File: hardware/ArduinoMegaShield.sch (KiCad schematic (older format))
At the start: 54 parts, among them P1 CONN_01X02, P10 CONN_01X02, P11 CONN_01X02, P12 CONN_01X02, P13 CONN_01X02, P14 CONN_01X02, P15 CONN_01X02, P16 CONN_01X02, P18 CONN_01X02, P2 CONN_01X02, P3 CONN_01X02, P4 CONN_01X02, P5 CONN_01X02, P6 CONN_01X02, P7 CONN_01X02, P8 CONN_01X02, P9 CONN_01X02, U1 A4988, U2 A4988, U3 A4988

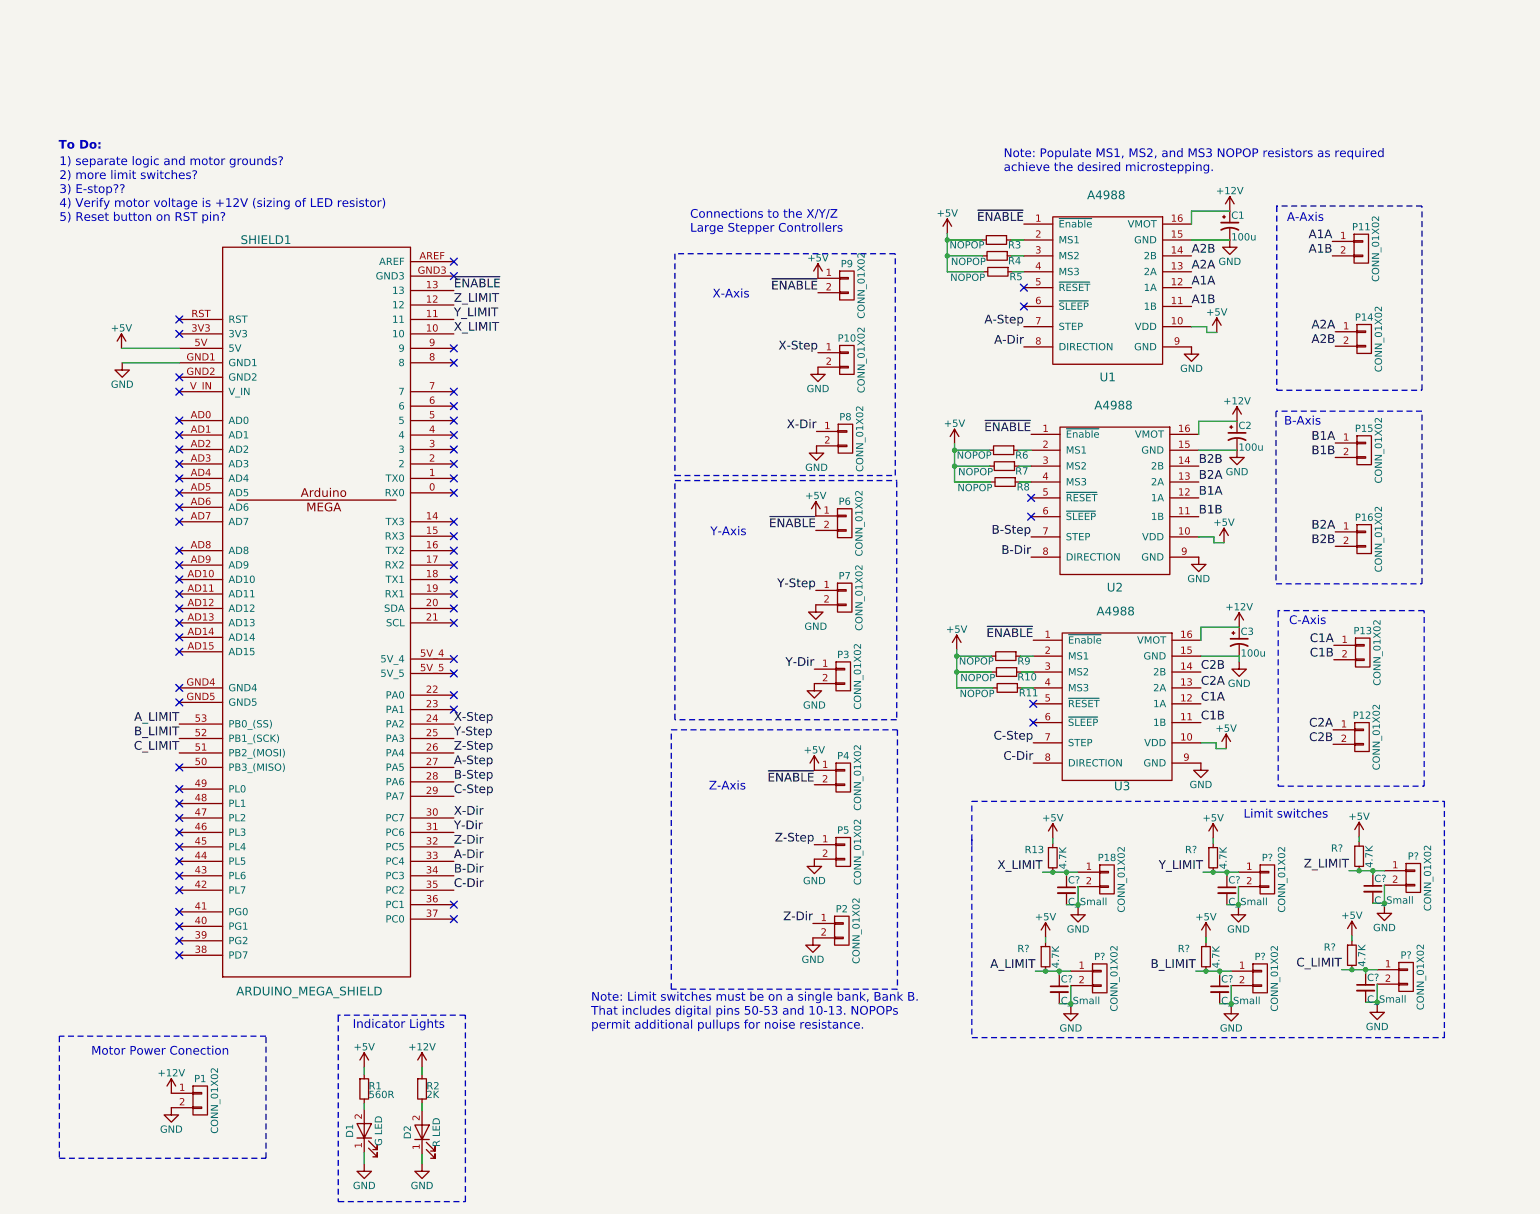
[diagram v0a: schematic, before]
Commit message: added estop on the avr reset pin
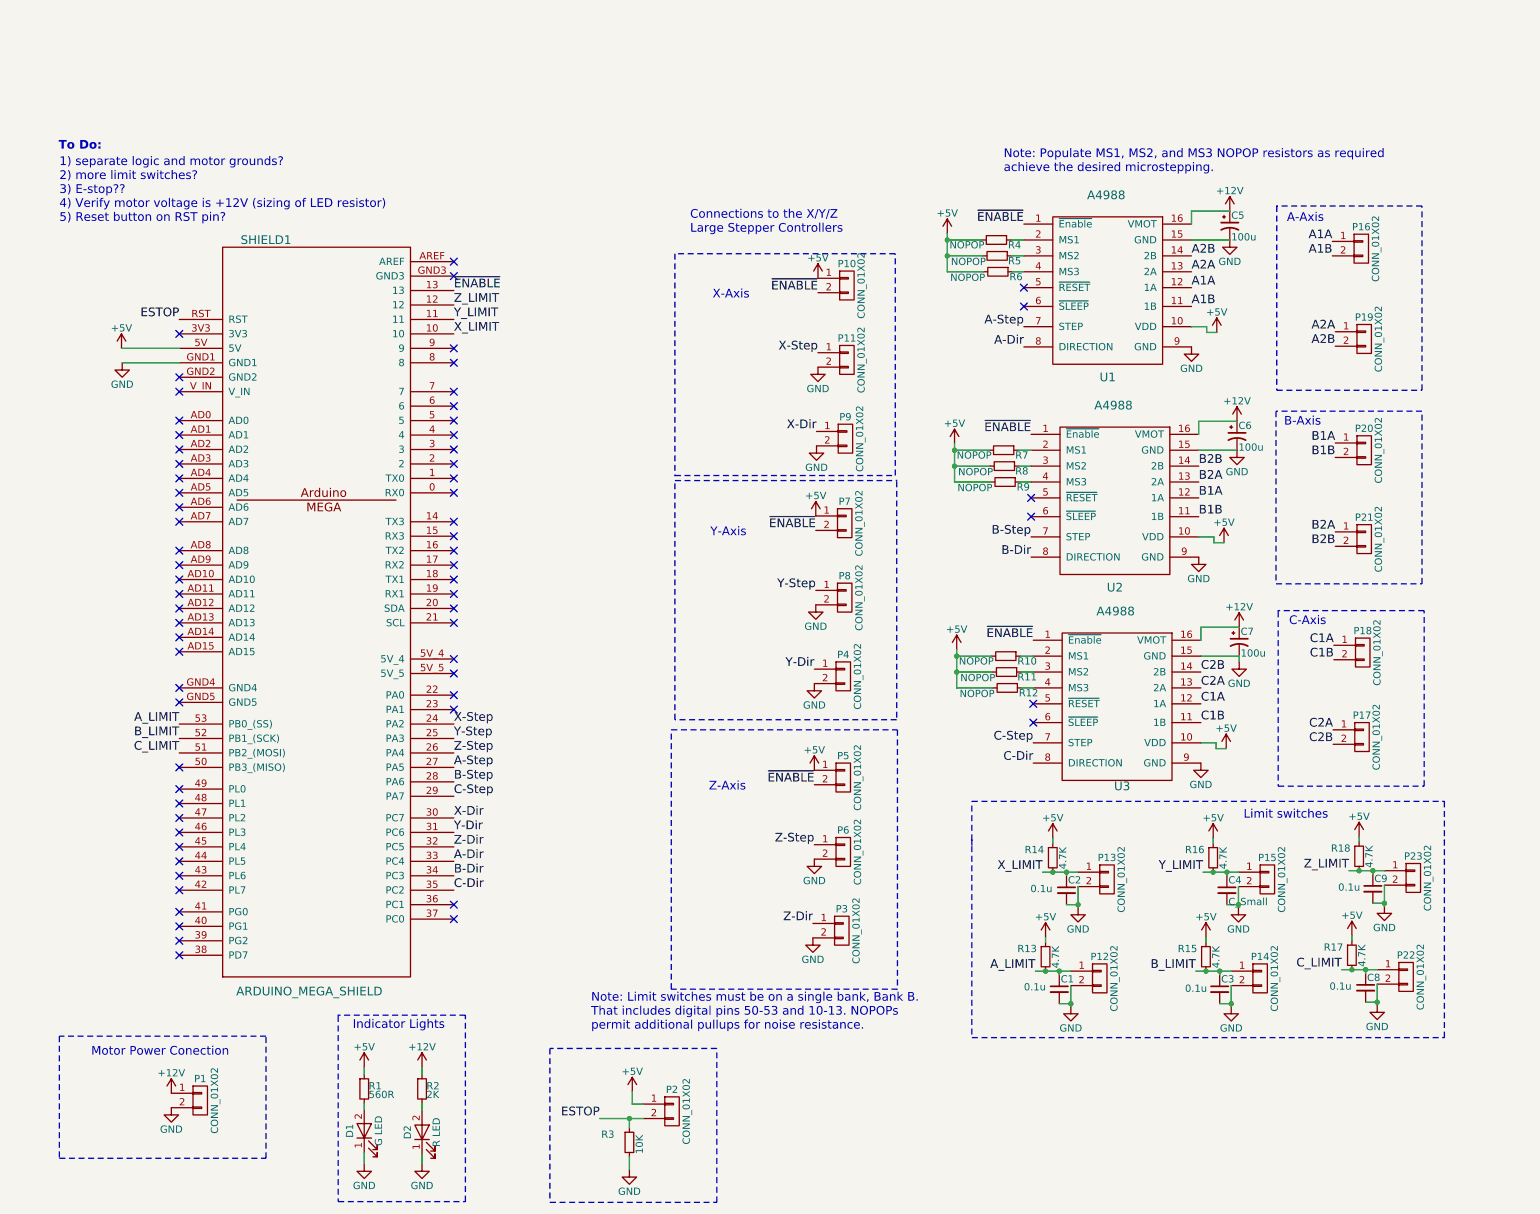
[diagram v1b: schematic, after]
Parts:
- added P2: CONN_01X02, 6axis:Terminal_Block_200_mil, symbol CONN_01X02
- added R3: 10K, Resistors_SMD:R_0805_HandSoldering, symbol R_Small
- C1, C2, C3, C8, C9: renamed from C?; value C_Small -> 0.1u; Fieldname (none) -> Value
- gave numbers to parts that had none: 11
- renumbered C1 to C5, C2 to C6, C3 to C7, P9 to P10, P10 to P11, P18 to P13, P11 to P16, P12 to P17, P13 to P18, P14 to P19, P15 to P20, P16 to P21, P2 to P3, P3 to P4, P4 to P5, P5 to P6, P6 to P7, P7 to P8, P8 to P9, R9 to R10, R10 to R11, R11 to R12, R13 to R14, R3 to R4, R4 to R5, R5 to R6, R6 to R7, R7 to R8, R8 to R9
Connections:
- net +5V: now also P2.1 (P1)
- net GND: now also R3.2
- net ESTOP: now reaches SHIELD1.RST
- net ESTOP: now also P2.2 (P2), R3.1
- no-connect marks 67 -> 66

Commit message: added safety-door switch as a halt-but-don't-downpower option
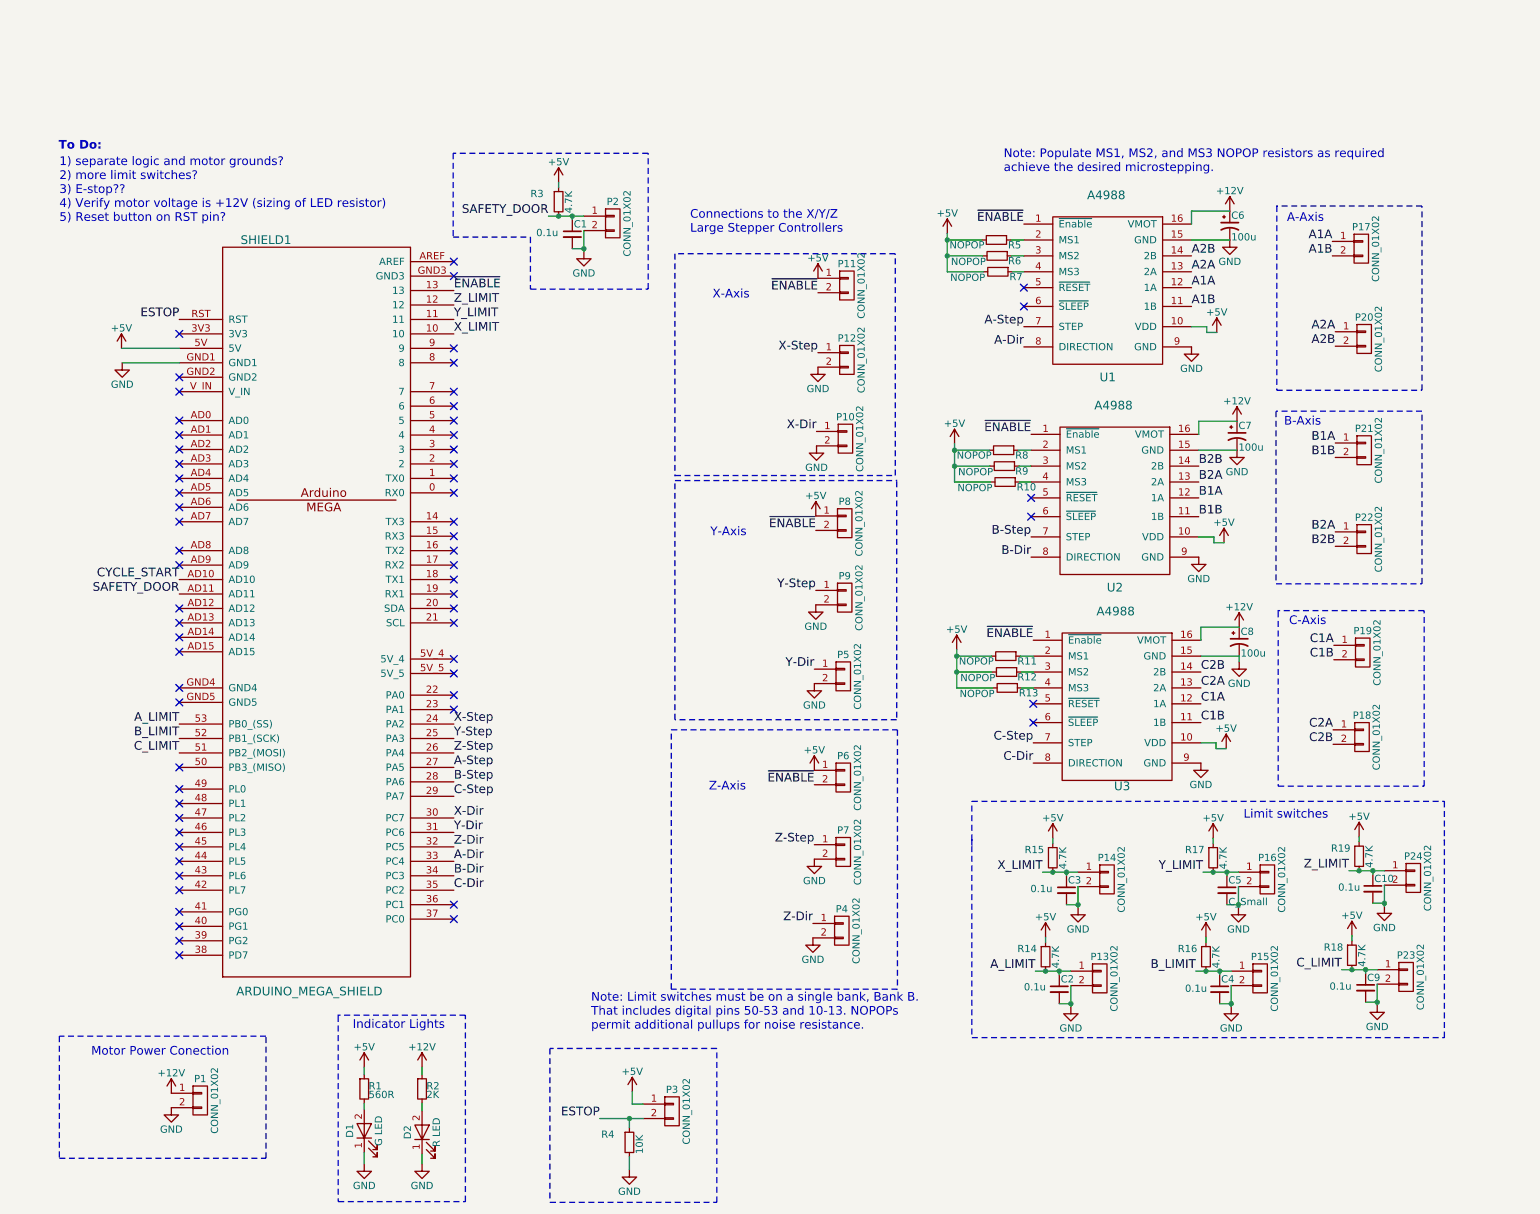
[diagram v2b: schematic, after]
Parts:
- added C1: 0.1u, symbol C_Small
- added P2: CONN_01X02, 6axis:Terminal_Block_200_mil, symbol CONN_01X02
- added R3: 4.7K, Resistors_SMD:R_0805_HandSoldering, symbol R_Small
- renumbered C9 to C10, C1 to C2, C2 to C3, C3 to C4, C4 to C5, C5 to C6, C6 to C7, C7 to C8, C8 to C9, P9 to P10, P10 to P11, P11 to P12, P12 to P13, P13 to P14, P14 to P15, P15 to P16, P16 to P17, P17 to P18, P18 to P19, P19 to P20, P20 to P21, P21 to P22, P22 to P23, P23 to P24, P2 to P3, P3 to P4, P4 to P5, P5 to P6, P6 to P7, P7 to P8, P8 to P9, R9 to R10, R10 to R11, R11 to R12, R12 to R13, R13 to R14, R14 to R15, R15 to R16, R16 to R17, R17 to R18, R18 to R19, R3 to R4, R4 to R5, R5 to R6, R6 to R7, R7 to R8, R8 to R9
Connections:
- net +5V: now also R3.1
- net GND: now also C1.2, P2.2 (P2)
- net CYCLE_START: now reaches SHIELD1.AD10
- net SAFETY_DOOR: now reaches SHIELD1.AD11
- net SAFETY_DOOR: now also C1.1, P2.1 (P1), R3.2
- no-connect marks 66 -> 64

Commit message: changed pull down resistor to 4.7k and added note about rotary dip switch
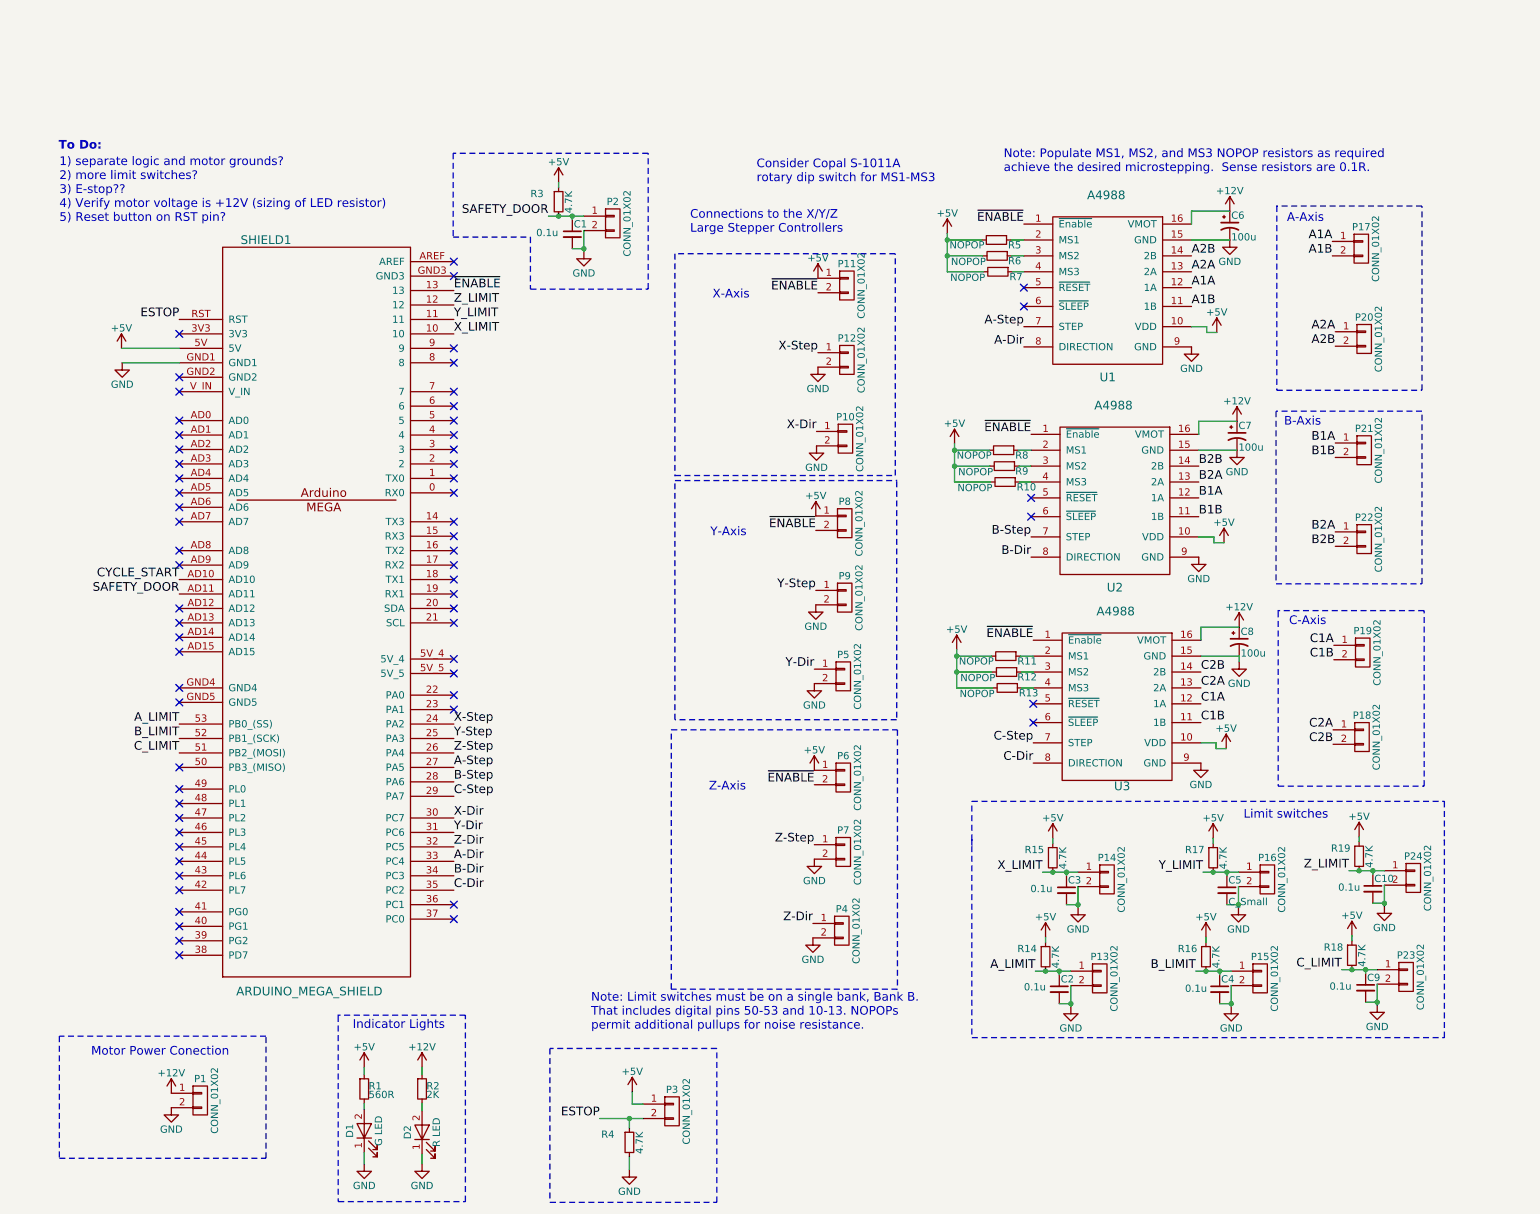
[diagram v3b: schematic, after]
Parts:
- R4: value 10K -> 4.7K
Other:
- note added: "Consider Copal S-1011A\nrotary dip switch for MS1-MS3"
- note added: "Note: Populate MS1, MS2, and MS3 NOPOP resistors as required\nachieve the desired microstepping. Sense resistors are 0.1R."
- note removed: "Note: Populate MS1, MS2, and MS3 NOPOP resistors as required\nachieve the desired microstepping."
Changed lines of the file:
@@
 C_LIMIT
 Text Notes 7255 720  0    60   ~ 0
-Note: Populate MS1, MS2, and MS3 NOPOP resistors as required\nachieve the desired microstepping.
+Note: Populate MS1, MS2, and MS3 NOPOP resistors as required\nachieve the desired microstepping.  Sense resistors are 0.1R.
 $Comp
 L GND #PWR21
@@
 P 4665 7425
 F 0 "R4" H 4470 7480 50  0000 L CNN
-F 1 "10K" V 4735 7345 50  0000 L CNN
+F 1 "4.7K" V 4735 7345 50  0000 L CNN
 F 2 "Resistors_SMD:R_0805_HandSoldering" H 4665 7425 50  0001 C CNN
 F 3 "" H 4665 7425 50  0000 C CNN
@@
 Text Label 1550 3530 2    60   ~ 0
 CYCLE_START
+Text Notes 5545 790  0    60   ~ 0
+Consider Copal S-1011A\nrotary dip switch for MS1-MS3
 $EndSCHEMATC

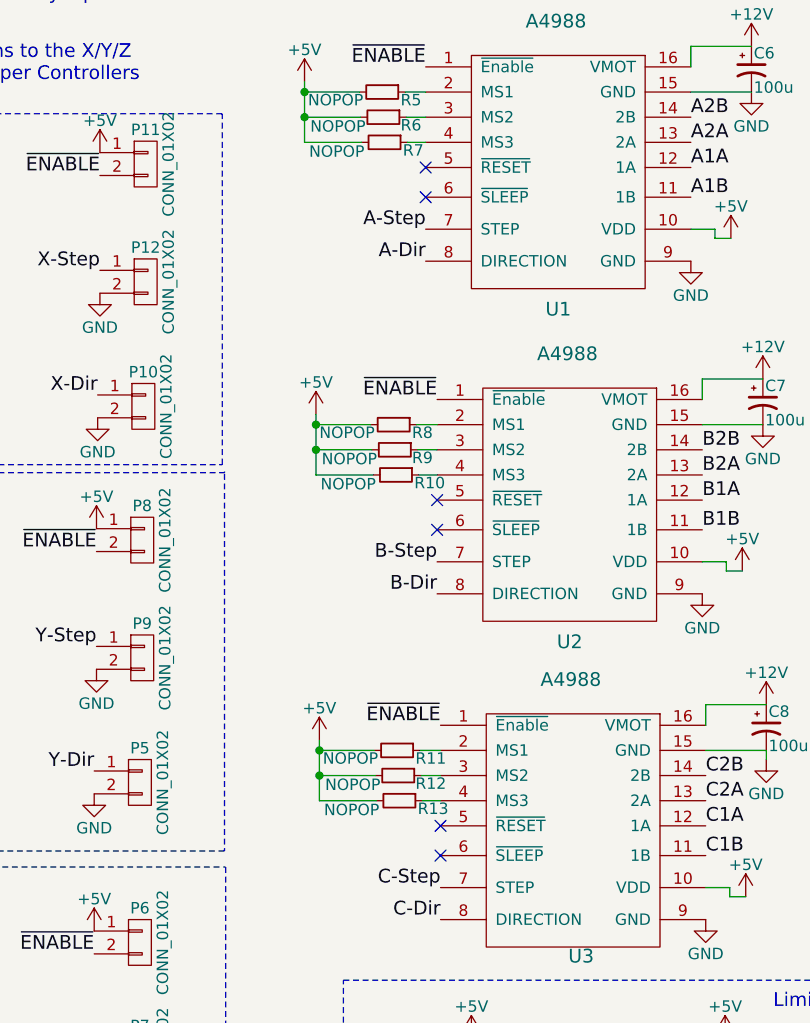
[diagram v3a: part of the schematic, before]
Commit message: wired ~SLEEP and ~RESET together on small stepper drivers
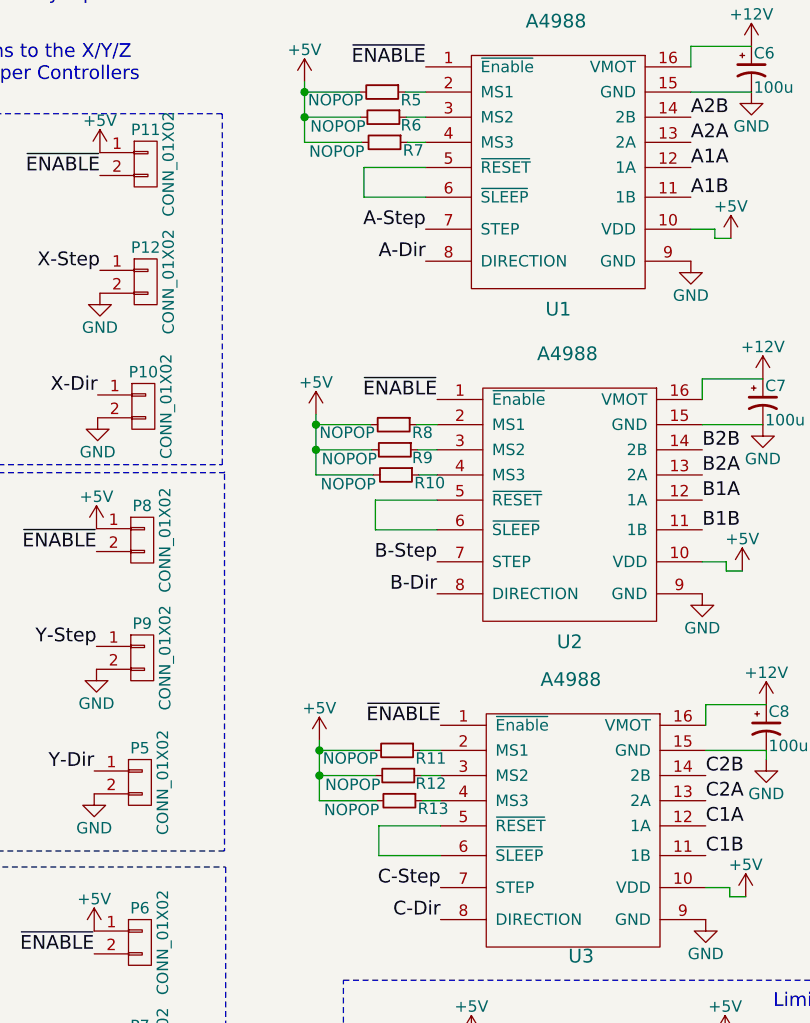
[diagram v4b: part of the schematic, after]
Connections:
- net at U1.5 (~RESET): now also U1.6 (~SLEEP)
- net at U2.5 (~RESET): now also U2.6 (~SLEEP)
- net at U3.5 (~RESET): now also U3.6 (~SLEEP)
- no-connect marks 64 -> 58
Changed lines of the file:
@@
 Text Label 7460 4660 2    60   ~ 0
 C-Step
-NoConn ~ 7460 4520
-NoConn ~ 7460 4390
-NoConn ~ 7445 2965
-NoConn ~ 7445 3095
-NoConn ~ 7395 1510
-NoConn ~ 7395 1640
 $Comp
 L CONN_01X02 P1
@@
 Text Notes 5545 790  0    60   ~ 0
 Consider Copal S-1011A\nrotary dip switch for MS1-MS3
+Wire Wire Line
+	7395 1510 7125 1510
+Wire Wire Line
+	7125 1510 7125 1640
+Wire Wire Line
+	7125 1640 7395 1640
+Wire Wire Line
+	7445 2965 7175 2965
+Wire Wire Line
+	7175 2965 7175 3095
+Wire Wire Line
+	7175 3095 7445 3095
+Wire Wire Line
+	7460 4390 7190 4390
+Wire Wire Line
+	7190 4390 7190 4520
+Wire Wire Line
+	7190 4520 7460 4520
 $EndSCHEMATC
